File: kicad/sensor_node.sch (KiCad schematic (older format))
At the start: 5 parts

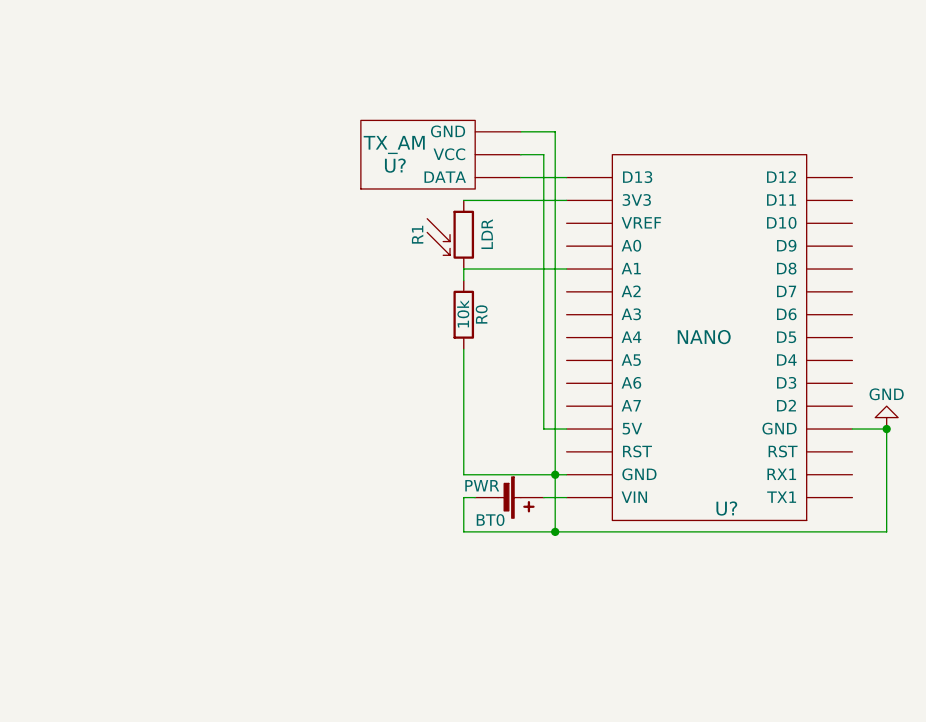
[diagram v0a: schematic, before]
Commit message: Código dos sensor nodes adicionado
Além disso foi atualizado o esquemático dos sensor nodes.
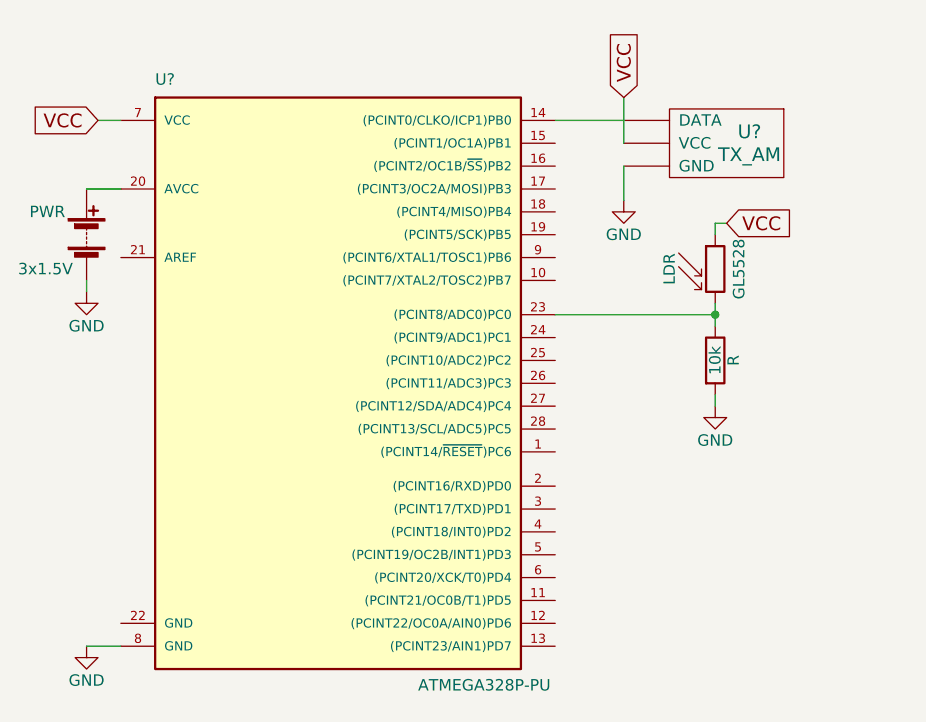
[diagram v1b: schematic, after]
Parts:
- removed BT0: PWR, symbol Battery_Cell
- removed R0: 10k, symbol R
- removed R1: LDR, Opto-Devices:Resistor_LDR_10x8.5_RM7.6, symbol LDR03
- removed U?: NANO, symbol NANO
- removed U?: TX_AM, symbol TX_AM
- added LDR: GL5528, Opto-Devices:Resistor_LDR_10x8.5_RM7.6, symbol LDR03
- added PWR: 3x1.5V, symbol Battery
- added R: 10k, symbol R
- added U?: ATMEGA328P-PU, DIL28, symbol ATMEGA328P-PU
- added U?: TX_AM, symbol TX_AM
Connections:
- net GND: now also PWR.2 (-), R.2, U?.8 (GND), U?.~ (VCC)
- new net: U?.14 ((PCINT0/CLKO/ICP1)PB0), U?.~ (VCC)
- new net: PWR.1 (+), U?.20 (AVCC)
- new net: LDR.2, R.1, U?.23 ((PCINT8/ADC0)PC0)
- new net VCC: LDR.1, U?.7 (VCC), U?.~ (VCC)
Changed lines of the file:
@@
 LIBS:valves
 LIBS:nano
+LIBS:sensor_node-cache
 EELAYER 25 0
 EELAYER END
@@
 Title "Sensor Node"
 Date "2018-03-21"
-Rev "1.0"
+Rev "1.1"
 Comp ""
 Comment1 ""
@@
 $EndDescr
 $Comp
-L NANO U?
-U 1 1 5AB2C710
-P 6000 3200
-F 0 "U?" H 6100 2500 60  0000 C CNN
-F 1 "NANO" H 6000 3250 60  0000 C CNN
-F 2 "" H 6000 3200 60  0001 C CNN
-F 3 "" H 6000 3200 60  0001 C CNN
-	1    6000 3200
+L ATMEGA328P-PU U?
+U 1 1 5AC022DD
+P 4350 3300
+F 0 "U?" H 3600 4550 50  0000 L BNN
+F 1 "ATMEGA328P-PU" H 4750 1900 50  0000 L BNN
+F 2 "DIL28" H 4350 3300 50  0001 C CIN
+F 3 "" H 4350 3300 50  0001 C CNN
+	1    4350 3300
+	1    0    0    -1
+$EndComp
+$Comp
+L GND #PWR?
+U 1 1 5AC024E6
+P 6050 3450
+F 0 "#PWR?" H 6050 3200 50  0001 C CNN
+F 1 "GND" H 6050 3300 50  0000 C CNN
+F 2 "" H 6050 3450 50  0001 C CNN
+F 3 "" H 6050 3450 50  0001 C CNN
+	1    6050 3450
 	1    0    0    -1
 $EndComp
 $Comp
 L TX_AM U?
-U 1 1 5AB2C7CA
-P 4400 2700
-F 0 "U?" H 4650 3000 60  0000 C CNN
-F 1 "TX_AM" H 4650 3100 60  0000 C CNN
-F 2 "" H 4800 3050 60  0001 C CNN
-F 3 "" H 4800 3050 60  0001 C CNN
-	1    4400 2700
+U 1 1 5AC026ED
+P 6450 1950
+F 0 "U?" H 6700 2250 60  0000 C CNN
+F 1 "TX_AM" H 6700 2350 60  0000 C CNN
+F 2 "" H 6850 2300 60  0001 C CNN
+F 3 "" H 6850 2300 60  0001 C CNN
+	1    6450 1950
+	-1   0    0    1
+$EndComp
+Text GLabel 5650 2100 1    60   Input ~ 0
+VCC
+$Comp
+L GND #PWR?
+U 1 1 5AC02A06
+P 5650 2550
+F 0 "#PWR?" H 5650 2300 50  0001 C CNN
+F 1 "GND" H 5650 2400 50  0000 C CNN
+F 2 "" H 5650 2550 50  0001 C CNN
+F 3 "" H 5650 2550 50  0001 C CNN
+	1    5650 2550
+	1    0    0    -1
+$EndComp
+$Comp
+L Battery PWR
+U 1 1 5AC02AA1
+P 3300 2700
+F 0 "PWR" H 3050 2800 50  0000 L CNN
+F 1 "3x1.5V" H 3000 2550 50  0000 L CNN
+F 2 "" V 3300 2760 50  0001 C CNN
+F 3 "" V 3300 2760 50  0001 C CNN
+	1    3300 2700
+	1    0    0    -1
+$EndComp
+$Comp
+L GND #PWR?
+U 1 1 5AC02BE8
+P 3300 2950
+F 0 "#PWR?" H 3300 2700 50  0001 C CNN
+F 1 "GND" H 3300 2800 50  0000 C CNN
+F 2 "" H 3300 2950 50  0001 C CNN
+F 3 "" H 3300 2950 50  0001 C CNN
+	1    3300 2950
+	1    0    0    -1
+$EndComp
+$Comp
+L GND #PWR?
+U 1 1 5AC02C12
+P 3300 4500
+F 0 "#PWR?" H 3300 4250 50  0001 C CNN
+F 1 "GND" H 3300 4350 50  0000 C CNN
+F 2 "" H 3300 4500 50  0001 C CNN
+F 3 "" H 3300 4500 50  0001 C CNN
+	1    3300 4500
 	1    0    0    -1
 $EndComp
 Wire Wire Line
-	4950 3750 5400 3750
+	6050 3400 6050 3450
 Wire Wire Line
-	5350 2250 5350 4000
+	5350 2200 5650 2200
 Wire Wire Line
-	5300 3550 5400 3550
+	5650 2300 5650 2100
 Wire Wire Line
-	5300 2350 5300 3550
+	5650 2550 5650 2400
 Wire Wire Line
-	5350 2250 5200 2250
+	3300 2950 3300 2900
 Wire Wire Line
-	5200 2350 5300 2350
+	3300 4500 3450 4500
 Wire Wire Line
-	5200 2450 5400 2450
+	3300 2500 3450 2500
+Connection ~ 6050 3050
 $Comp
-L GND #PWR?
-U 1 1 5AB2CA3C
-P 6800 3550
-F 0 "#PWR?" H 6800 3300 50  0001 C CNN
-F 1 "GND" H 6800 3400 50  0000 C CNN
-F 2 "" H 6800 3550 50  0001 C CNN
-F 3 "" H 6800 3550 50  0001 C CNN
-	1    6800 3550
-	-1   0    0    1
-$EndComp
-Connection ~ 6800 3550
-Connection ~ 5350 3750
-$Comp
-L LDR03 R1
-U 1 1 5AB2CBA5
-P 4950 2700
-F 0 "R1" V 4750 2700 50  0000 C CNN
-F 1 "LDR" V 5025 2700 50  0000 C TNN
-F 2 "Opto-Devices:Resistor_LDR_10x8.5_RM7.6" V 5125 2700 50  0001 C CNN
-F 3 "" H 4950 2650 50  0001 C CNN
-	1    4950 2700
+L R R
+U 1 1 5AC02440
+P 6050 3250
+F 0 "R" V 6130 3250 50  0000 C CNN
+F 1 "10k" V 6050 3250 50  0000 C CNN
+F 2 "" V 5980 3250 50  0001 C CNN
+F 3 "" H 6050 3250 50  0001 C CNN
+	1    6050 3250
 	1    0    0    -1
 $EndComp
 Wire Wire Line
-	5400 2550 4950 2550
+	6050 3000 6050 3100
+Wire Wire Line
+	6050 2700 6050 2650
 $Comp
-L R R0
-U 1 1 5AB2CC2D
-P 4950 3050
-F 0 "R0" V 5030 3050 50  0000 C CNN
-F 1 "10k" V 4950 3050 50  0000 C CNN
-F 2 "" V 4880 3050 50  0001 C CNN
-F 3 "" H 4950 3050 50  0001 C CNN
-	1    4950 3050
+L LDR03 LDR
+U 1 1 5AC02532
+P 6050 2850
+F 0 "LDR" V 5850 2850 50  0000 C CNN
+F 1 "GL5528" V 6125 2850 50  0000 C TNN
+F 2 "Opto-Devices:Resistor_LDR_10x8.5_RM7.6" V 6225 2850 50  0001 C CNN
+F 3 "" H 6050 2800 50  0001 C CNN
+	1    6050 2850
 	1    0    0    -1
 $EndComp
+Text GLabel 6100 2650 2    60   Input ~ 0
+VCC
 Wire Wire Line
-	4950 2850 4950 2900
+	6050 2650 6100 2650
 Wire Wire Line
-	5400 2850 4950 2850
+	5350 3050 6050 3050
+Text GLabel 3350 2200 0    60   Input ~ 0
+VCC
 Wire Wire Line
-	4950 3750 4950 3200
-$Comp
-L Battery_Cell BT0
-U 1 1 5AB2CD39
-P 5100 3850
-F 0 "BT0" V 5200 3750 50  0000 L CNN
-F 1 "PWR" V 5050 3700 50  0000 L CNN
-F 2 "" V 5100 3910 50  0001 C CNN
-F 3 "" V 5100 3910 50  0001 C CNN
-	1    5100 3850
-	0    1    1    0
-$EndComp
-Wire Wire Line
-	5400 3850 5300 3850
-Wire Wire Line
-	5000 3850 4950 3850
-Wire Wire Line
-	4950 3850 4950 4000
-Connection ~ 5350 4000
-Wire Wire Line
-	6650 3550 6800 3550
-Wire Wire Line
-	6800 4000 6800 3550
-Wire Wire Line
-	4950 4000 6800 4000
+	3350 2200 3450 2200
 $EndSCHEMATC

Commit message: Apenas arquivos necessários deixados no repositório
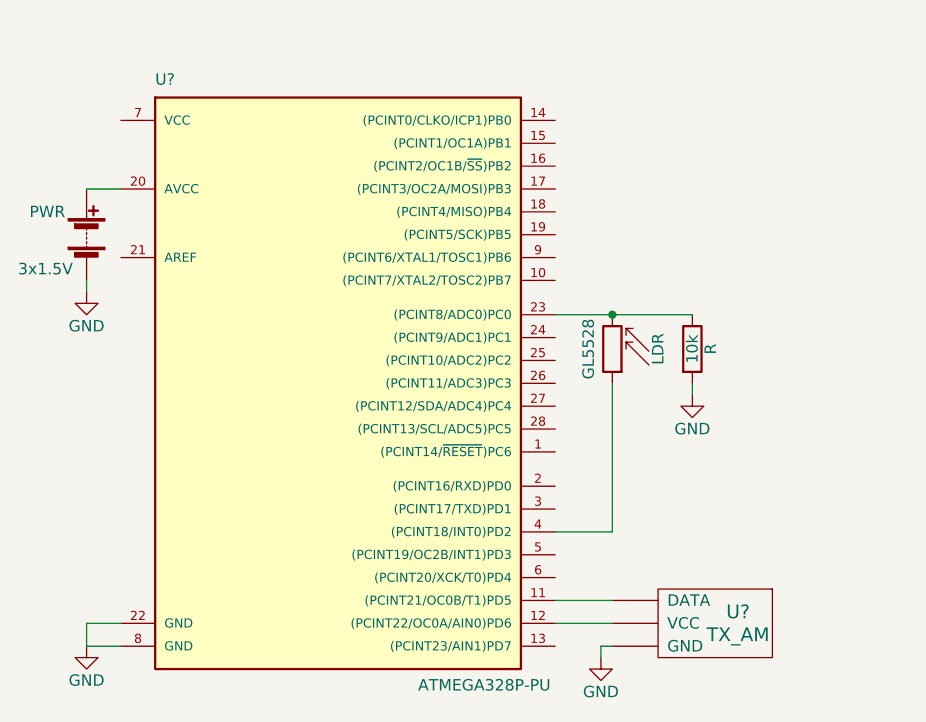
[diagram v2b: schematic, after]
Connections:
- net GND: now also U?.22 (GND)
- net at U?.11 ((PCINT21/OC0B/T1)PD5): now also U?.~ (VCC)
- net at U?.12 ((PCINT22/OC0A/AIN0)PD6): now also U?.~ (VCC)
- net at U?.14 ((PCINT0/CLKO/ICP1)PB0): no longer U?.~ (VCC)
- net at U?.4 ((PCINT18/INT0)PD2): now also LDR.1
- removed net VCC: LDR.1, U?.7 (VCC), U?.~ (VCC)
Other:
- moved on the sheet: LDR, R, U?
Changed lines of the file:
@@
-$EndComp
-$Comp
-L GND #PWR?
-U 1 1 5AC024E6
-P 6050 3450
-F 0 "#PWR?" H 6050 3200 50  0001 C CNN
-F 1 "GND" H 6050 3300 50  0000 C CNN
-F 2 "" H 6050 3450 50  0001 C CNN
-F 3 "" H 6050 3450 50  0001 C CNN
-	1    6050 3450
-	1    0    0    -1
 $EndComp
 $Comp
 L TX_AM U?
 U 1 1 5AC026ED
-P 6450 1950
-F 0 "U?" H 6700 2250 60  0000 C CNN
-F 1 "TX_AM" H 6700 2350 60  0000 C CNN
-F 2 "" H 6850 2300 60  0001 C CNN
-F 3 "" H 6850 2300 60  0001 C CNN
-	1    6450 1950
+P 6400 4050
+F 0 "U?" H 6650 4350 60  0000 C CNN
+F 1 "TX_AM" H 6650 4450 60  0000 C CNN
+F 2 "" H 6800 4400 60  0001 C CNN
+F 3 "" H 6800 4400 60  0001 C CNN
+	1    6400 4050
 	-1   0    0    1
-$EndComp
-Text GLabel 5650 2100 1    60   Input ~ 0
-VCC
-$Comp
-L GND #PWR?
-U 1 1 5AC02A06
-P 5650 2550
-F 0 "#PWR?" H 5650 2300 50  0001 C CNN
-F 1 "GND" H 5650 2400 50  0000 C CNN
-F 2 "" H 5650 2550 50  0001 C CNN
-F 3 "" H 5650 2550 50  0001 C CNN
-	1    5650 2550
-	1    0    0    -1
 $EndComp
 $Comp
@@
 	1    0    0    -1
 $EndComp
-Wire Wire Line
-	6050 3400 6050 3450
-Wire Wire Line
-	5350 2200 5650 2200
-Wire Wire Line
-	5650 2300 5650 2100
-Wire Wire Line
-	5650 2550 5650 2400
+$Comp
+L R R
+U 1 1 5AC02440
+P 5950 3200
+F 0 "R" V 6030 3200 50  0000 C CNN
+F 1 "10k" V 5950 3200 50  0000 C CNN
+F 2 "" V 5880 3200 50  0001 C CNN
+F 3 "" H 5950 3200 50  0001 C CNN
+	1    5950 3200
+	1    0    0    -1
+$EndComp
+$Comp
+L LDR03 LDR
+U 1 1 5AC02532
+P 5600 3200
+F 0 "LDR" V 5400 3200 50  0000 C CNN
+F 1 "GL5528" V 5675 3200 50  0000 C TNN
+F 2 "Opto-Devices:Resistor_LDR_10x8.5_RM7.6" V 5775 3200 50  0001 C CNN
+F 3 "" H 5600 3150 50  0001 C CNN
+	1    5600 3200
+	-1   0    0    1
+$EndComp
+$Comp
+L GND #PWR?
+U 1 1 5AD92E3C
+P 5950 3400
+F 0 "#PWR?" H 5950 3150 50  0001 C CNN
+F 1 "GND" H 5950 3250 50  0000 C CNN
+F 2 "" H 5950 3400 50  0001 C CNN
+F 3 "" H 5950 3400 50  0001 C CNN
+	1    5950 3400
+	1    0    0    -1
+$EndComp
 Wire Wire Line
 	3300 2950 3300 2900
@@
 Wire Wire Line
 	3300 2500 3450 2500
-Connection ~ 6050 3050
+Wire Wire Line
+	3300 4500 3300 4400
+Wire Wire Line
+	3300 4400 3450 4400
+Connection ~ 5600 3050
+Wire Wire Line
+	5950 3400 5950 3350
+Wire Wire Line
+	5350 3050 5950 3050
+Wire Wire Line
+	5350 4000 5600 4000
+Wire Wire Line
+	5600 4000 5600 3350
+Wire Wire Line
+	5350 4300 5600 4300
+Wire Wire Line
+	5350 4400 5600 4400
 $Comp
-L R R
-U 1 1 5AC02440
-P 6050 3250
-F 0 "R" V 6130 3250 50  0000 C CNN
-F 1 "10k" V 6050 3250 50  0000 C CNN
-F 2 "" V 5980 3250 50  0001 C CNN
-F 3 "" H 6050 3250 50  0001 C CNN
-	1    6050 3250
+L GND #PWR?
+U 1 1 5AD9320B
+P 5550 4550
+F 0 "#PWR?" H 5550 4300 50  0001 C CNN
+F 1 "GND" H 5550 4400 50  0000 C CNN
+F 2 "" H 5550 4550 50  0001 C CNN
+F 3 "" H 5550 4550 50  0001 C CNN
+	1    5550 4550
 	1    0    0    -1
 $EndComp
 Wire Wire Line
-	6050 3000 6050 3100
+	5550 4550 5550 4500
 Wire Wire Line
-	6050 2700 6050 2650
-$Comp
-L LDR03 LDR
-U 1 1 5AC02532
-P 6050 2850
-F 0 "LDR" V 5850 2850 50  0000 C CNN
-F 1 "GL5528" V 6125 2850 50  0000 C TNN
-F 2 "Opto-Devices:Resistor_LDR_10x8.5_RM7.6" V 6225 2850 50  0001 C CNN
-F 3 "" H 6050 2800 50  0001 C CNN
-	1    6050 2850
-	1    0    0    -1
-$EndComp
-Text GLabel 6100 2650 2    60   Input ~ 0
-VCC
-Wire Wire Line
-	6050 2650 6100 2650
-Wire Wire Line
-	5350 3050 6050 3050
-Text GLabel 3350 2200 0    60   Input ~ 0
-VCC
-Wire Wire Line
-	3350 2200 3450 2200
+	5550 4500 5600 4500
 $EndSCHEMATC

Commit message: Esquemático do sensor node atualizado
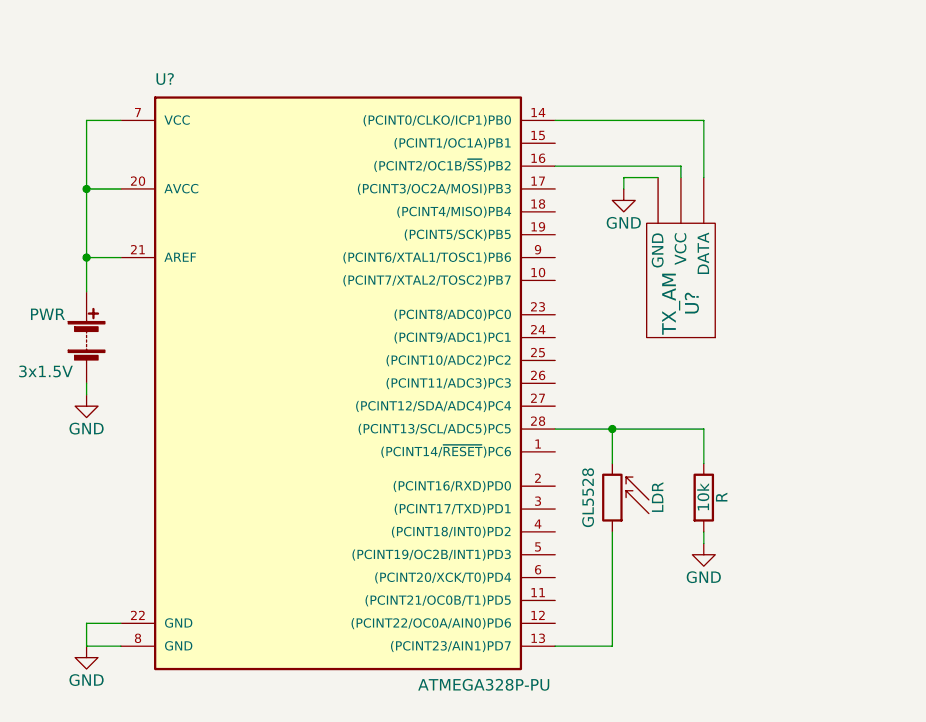
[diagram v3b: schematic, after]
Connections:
- net at U?.11 ((PCINT21/OC0B/T1)PD5): no longer U?.~ (VCC)
- net at U?.12 ((PCINT22/OC0A/AIN0)PD6): no longer U?.~ (VCC)
- net at U?.13 ((PCINT23/AIN1)PD7): now also LDR.1
- net at U?.14 ((PCINT0/CLKO/ICP1)PB0): now also U?.~ (VCC)
- net at U?.16 ((PCINT2/OC1B/~SS~)PB2): now also U?.~ (VCC)
- net at PWR.1 (+), U?.20 (AVCC): now also U?.21 (AREF), U?.7 (VCC)
- net at LDR.2, R.1: now also U?.28 ((PCINT13/SCL/ADC5)PC5); no longer U?.23 ((PCINT8/ADC0)PC0)
- net at U?.4 ((PCINT18/INT0)PD2): no longer LDR.1
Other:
- moved on the sheet: LDR, PWR, R, U?
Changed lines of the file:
@@
 L TX_AM U?
 U 1 1 5AC026ED
-P 6400 4050
-F 0 "U?" H 6650 4350 60  0000 C CNN
-F 1 "TX_AM" H 6650 4450 60  0000 C CNN
-F 2 "" H 6800 4400 60  0001 C CNN
-F 3 "" H 6800 4400 60  0001 C CNN
-	1    6400 4050
-	-1   0    0    1
+P 6250 3250
+F 0 "U?" H 6500 3550 60  0000 C CNN
+F 1 "TX_AM" H 6500 3650 60  0000 C CNN
+F 2 "" H 6650 3600 60  0001 C CNN
+F 3 "" H 6650 3600 60  0001 C CNN
+	1    6250 3250
+	0    -1   -1   0
 $EndComp
 $Comp
 L Battery PWR
 U 1 1 5AC02AA1
-P 3300 2700
-F 0 "PWR" H 3050 2800 50  0000 L CNN
-F 1 "3x1.5V" H 3000 2550 50  0000 L CNN
-F 2 "" V 3300 2760 50  0001 C CNN
-F 3 "" V 3300 2760 50  0001 C CNN
-	1    3300 2700
+P 3300 3150
+F 0 "PWR" H 3050 3250 50  0000 L CNN
+F 1 "3x1.5V" H 3000 3000 50  0000 L CNN
+F 2 "" V 3300 3210 50  0001 C CNN
+F 3 "" V 3300 3210 50  0001 C CNN
+	1    3300 3150
 	1    0    0    -1
 $EndComp
@@
 L GND #PWR?
 U 1 1 5AC02BE8
-P 3300 2950
-F 0 "#PWR?" H 3300 2700 50  0001 C CNN
-F 1 "GND" H 3300 2800 50  0000 C CNN
-F 2 "" H 3300 2950 50  0001 C CNN
-F 3 "" H 3300 2950 50  0001 C CNN
-	1    3300 2950
+P 3300 3400
+F 0 "#PWR?" H 3300 3150 50  0001 C CNN
+F 1 "GND" H 3300 3250 50  0000 C CNN
+F 2 "" H 3300 3400 50  0001 C CNN
+F 3 "" H 3300 3400 50  0001 C CNN
+	1    3300 3400
 	1    0    0    -1
 $EndComp
@@
 L R R
 U 1 1 5AC02440
-P 5950 3200
-F 0 "R" V 6030 3200 50  0000 C CNN
-F 1 "10k" V 5950 3200 50  0000 C CNN
-F 2 "" V 5880 3200 50  0001 C CNN
-F 3 "" H 5950 3200 50  0001 C CNN
-	1    5950 3200
+P 6000 3850
+F 0 "R" V 6080 3850 50  0000 C CNN
+F 1 "10k" V 6000 3850 50  0000 C CNN
+F 2 "" V 5930 3850 50  0001 C CNN
+F 3 "" H 6000 3850 50  0001 C CNN
+	1    6000 3850
 	1    0    0    -1
 $EndComp
@@
 L LDR03 LDR
 U 1 1 5AC02532
-P 5600 3200
-F 0 "LDR" V 5400 3200 50  0000 C CNN
-F 1 "GL5528" V 5675 3200 50  0000 C TNN
-F 2 "Opto-Devices:Resistor_LDR_10x8.5_RM7.6" V 5775 3200 50  0001 C CNN
-F 3 "" H 5600 3150 50  0001 C CNN
-	1    5600 3200
+P 5600 3850
+F 0 "LDR" V 5400 3850 50  0000 C CNN
+F 1 "GL5528" V 5675 3850 50  0000 C TNN
+F 2 "Opto-Devices:Resistor_LDR_10x8.5_RM7.6" V 5775 3850 50  0001 C CNN
+F 3 "" H 5600 3800 50  0001 C CNN
+	1    5600 3850
 	-1   0    0    1
 $EndComp
@@
 L GND #PWR?
 U 1 1 5AD92E3C
-P 5950 3400
-F 0 "#PWR?" H 5950 3150 50  0001 C CNN
-F 1 "GND" H 5950 3250 50  0000 C CNN
-F 2 "" H 5950 3400 50  0001 C CNN
-F 3 "" H 5950 3400 50  0001 C CNN
-	1    5950 3400
+P 6000 4050
+F 0 "#PWR?" H 6000 3800 50  0001 C CNN
+F 1 "GND" H 6000 3900 50  0000 C CNN
+F 2 "" H 6000 4050 50  0001 C CNN
+F 3 "" H 6000 4050 50  0001 C CNN
+	1    6000 4050
+	1    0    0    -1
+$EndComp
+$Comp
+L GND #PWR?
+U 1 1 5AD9320B
+P 5650 2500
+F 0 "#PWR?" H 5650 2250 50  0001 C CNN
+F 1 "GND" H 5650 2350 50  0000 C CNN
+F 2 "" H 5650 2500 50  0001 C CNN
+F 3 "" H 5650 2500 50  0001 C CNN
+	1    5650 2500
 	1    0    0    -1
 $EndComp
 Wire Wire Line
-	3300 2950 3300 2900
+	3300 3400 3300 3350
 Wire Wire Line
 	3300 4500 3450 4500
@@
 Wire Wire Line
 	3300 4400 3450 4400
-Connection ~ 5600 3050
 Wire Wire Line
-	5950 3400 5950 3350
+	6000 4050 6000 4000
 Wire Wire Line
-	5350 3050 5950 3050
+	3300 2200 3300 2950
 Wire Wire Line
-	5350 4000 5600 4000
+	3300 2200 3450 2200
+Connection ~ 3300 2500
 Wire Wire Line
-	5600 4000 5600 3350
+	3450 2800 3300 2800
+Connection ~ 3300 2800
 Wire Wire Line
-	5350 4300 5600 4300
+	5350 2200 6000 2200
 Wire Wire Line
-	5350 4400 5600 4400
-$Comp
-L GND #PWR?
-U 1 1 5AD9320B
-P 5550 4550
-F 0 "#PWR?" H 5550 4300 50  0001 C CNN
-F 1 "GND" H 5550 4400 50  0000 C CNN
-F 2 "" H 5550 4550 50  0001 C CNN
-F 3 "" H 5550 4550 50  0001 C CNN
-	1    5550 4550
-	1    0    0    -1
-$EndComp
+	6000 2200 6000 2450
 Wire Wire Line
-	5550 4550 5550 4500
+	5350 2400 5900 2400
 Wire Wire Line
-	5550 4500 5600 4500
+	5900 2400 5900 2450
+Wire Wire Line
+	5650 2500 5650 2450
+Wire Wire Line
+	5650 2450 5800 2450
+Wire Wire Line
+	5600 4500 5600 4000
+Wire Wire Line
+	5600 3550 5600 3700
+Wire Wire Line
+	5350 4500 5600 4500
+Wire Wire Line
+	5350 3550 6000 3550
+Connection ~ 5600 3550
+Wire Wire Line
+	6000 3550 6000 3700
 $EndSCHEMATC
